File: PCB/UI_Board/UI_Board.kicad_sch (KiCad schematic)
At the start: 13 parts, among them J1 DISPLAY, J2 CABLE, SW1 SW_UP, SW2 SW_DWN, SW3 SW_PRE_1, SW4 SW_PRE_2

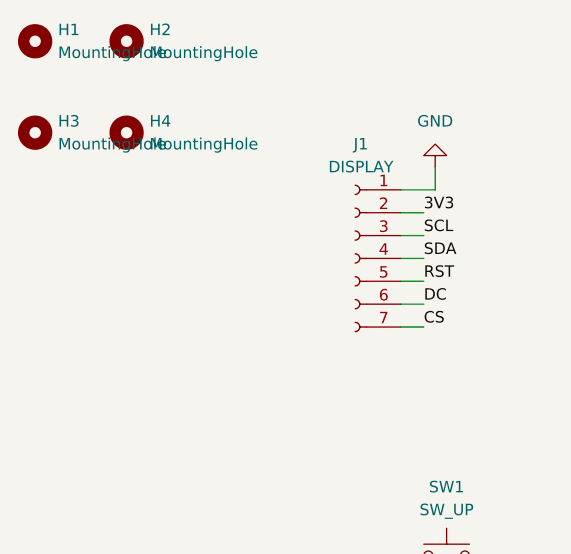
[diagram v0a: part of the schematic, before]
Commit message: chore: update UI board files and add build script
Update UI board KiCad project, schematic, and PCB. Add manufacturing
outputs (PDF, STEP, BOM). Add TFT display STEP model. Add
build_esp32s3.ps1 helper script for building under Windows PowerShell
without the IDF export.ps1 (works around MSYSTEM/py env mismatch).

Co-Authored-By: Claude Sonnet 4.6 <noreply@anthropic.com>
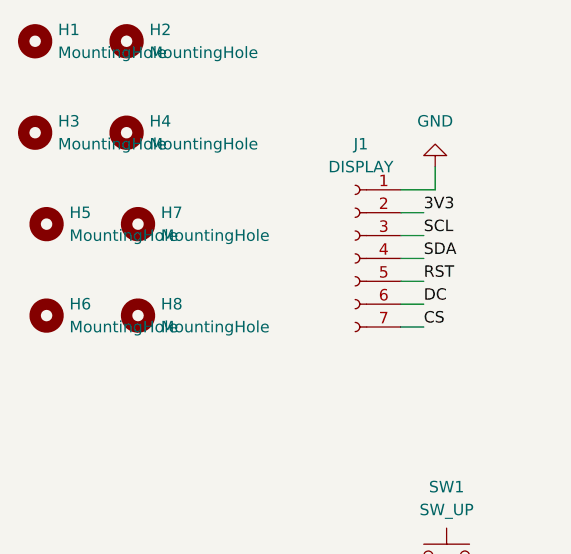
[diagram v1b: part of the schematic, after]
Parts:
- added H5, H6, H7, H8: MountingHole, MountingHole:MountingHole_3.2mm_M3, symbol Mechanical:MountingHole
